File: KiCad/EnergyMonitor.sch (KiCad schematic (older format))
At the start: 70 parts, among them J1 Conn_01x04, J10 AudioJack3_Ground_Switch_5_pin, J11 Conn_01x02, J13 Barrel_Jack_Switch, J14 Conn_01x04, J15 Conn_01x04, J16 4P4C, J2 Conn_01x04, J3 Conn_01x04, J4 Conn_01x04, J5 Conn_01x04, J6 Conn_01x04, J7 Conn_01x02, J8 AudioJack3_Ground_Switch_5_pin, J9 AudioJack3_Ground_Switch_5_pin, U1 ESP32_D1_MINI, U2 HT7333

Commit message: circuit design & pcb layout
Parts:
- R14: footprint LED_SMD:LED_0805_2012Metric -> Resistor_SMD:R_0805_2012Metric
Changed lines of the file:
@@
 F 0 "R14" H 5595 6896 50  0000 L CNN
 F 1 "4K7" H 5595 6805 50  0000 L CNN
-F 2 "LED_SMD:LED_0805_2012Metric" V 5455 6850 50  0001 C CNN
+F 2 "Resistor_SMD:R_0805_2012Metric" V 5455 6850 50  0001 C CNN
 F 3 "~" H 5525 6850 50  0001 C CNN
 	1    5525 6850

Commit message: circuit design & pcb layout
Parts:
- added R15, R30, R31, R32, R33: 0R, Resistor_SMD:R_0805_2012Metric, symbol Device:R
- J14: footprint Connector_JST:JST_SH_SM04B-SRSS-TB_1x04-1MP_P1.00mm_Horizontal -> Connector_JST:JST_SH_BM04B-SRSS-TB_1x04-1MP_P1.00mm_Vertical
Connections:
- net ADC1_CH4: now also U1.7 (IO35); no longer U1.33 (IO32)
- net ADC1_CH5: now also U1.33 (IO32); no longer U1.9 (IO33)
- net ADC1_CH7: now also U1.9 (IO33); no longer U1.7 (IO35)
- net GND: now also J13.2, J13.3, R15.1, R30.1, R31.1, R32.1, R33.1
- net GNDA: now also R15.2, R30.2, R31.2, R32.2, R33.2; no longer J13.2, J13.3
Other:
- note added: "Connector_JST:JST_SH_BM04B-SRSS-TB_1x04-1MP_P1.00mm_Vertical"
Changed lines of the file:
@@
 Sheet 1 1
 Title "ESP32 Energy Monitor"
-Date "2021-09-22"
+Date "2021-09-24"
 Rev "v1.0"
 Comp ""
@@
 Text GLabel 1650 2725 0    50   Input ~ 0
 ADC1_CH6
-Text GLabel 1650 2325 0    50   Input ~ 0
+Text GLabel 1650 2525 0    50   Input ~ 0
 ADC1_CH7
 Text Notes 9850 5200 0    50   ~ 0
@@
 	1    0    0    -1
 $EndComp
-$Comp
-L power:GNDA #PWR024
-U 1 1 613562F0
-P 8325 2400
-F 0 "#PWR024" H 8325 2150 50  0001 C CNN
-F 1 "GNDA" H 8330 2227 50  0000 C CNN
-F 2 "" H 8325 2400 50  0001 C CNN
-F 3 "" H 8325 2400 50  0001 C CNN
-	1    8325 2400
-	1    0    0    -1
-$EndComp
 Wire Wire Line
 	8175 2300 8325 2300
@@
 Text Notes 4000 7550 0    50   ~ 0
 Remove Jumper\nif ESP32 powered\nby USB.
-Text GLabel 1650 2525 0    50   Input ~ 0
-ADC1_CH5
 Text GLabel 2450 2425 2    50   Input ~ 0
+ADC1_CH5
+Text GLabel 1650 2325 0    50   Input ~ 0
 ADC1_CH4
 Text GLabel 2450 2125 2    50   Input ~ 0
@@
 F 0 "J14" H 8580 4842 50  0000 L CNN
 F 1 "Conn_01x04" H 8580 4751 50  0000 L CNN
-F 2 "Connector_JST:JST_SH_SM04B-SRSS-TB_1x04-1MP_P1.00mm_Horizontal" H 8500 4850 50  0001 C CNN
+F 2 "Connector_JST:JST_SH_BM04B-SRSS-TB_1x04-1MP_P1.00mm_Vertical" H 8500 4850 50  0001 C CNN
 F 3 "~" H 8500 4850 50  0001 C CNN
 	1    8500 4850
@@
 Text Notes 5875 7425 0    50   ~ 0
 red superbright LED\n0805 SMD\ngreen band -ve\n1k R => 1.4mA\n4K7 => 0.3mA\n@3.3v
+$Comp
+L power:GND #PWR0106
+U 1 1 6153C70C
+P 8325 2400
+F 0 "#PWR0106" H 8325 2150 50  0001 C CNN
+F 1 "GND" H 8330 2227 50  0000 C CNN
+F 2 "" H 8325 2400 50  0001 C CNN
+F 3 "" H 8325 2400 50  0001 C CNN
+	1    8325 2400
+	1    0    0    -1
+$EndComp
+$Comp
+L power:GND #PWR0107
+U 1 1 61546152
+P 8725 5850
+F 0 "#PWR0107" H 8725 5600 50  0001 C CNN
+F 1 "GND" H 8730 5677 50  0000 C CNN
+F 2 "" H 8725 5850 50  0001 C CNN
+F 3 "" H 8725 5850 50  0001 C CNN
+	1    8725 5850
+	1    0    0    -1
+$EndComp
+$Comp
+L power:GNDA #PWR0108
+U 1 1 61546DE3
+P 8425 5850
+F 0 "#PWR0108" H 8425 5600 50  0001 C CNN
+F 1 "GNDA" H 8430 5677 50  0000 C CNN
+F 2 "" H 8425 5850 50  0001 C CNN
+F 3 "" H 8425 5850 50  0001 C CNN
+	1    8425 5850
+	1    0    0    -1
+$EndComp
+Text Notes 12275 4825 0    50   ~ 0
+Connector_JST:JST_SH_BM04B-SRSS-TB_1x04-1MP_P1.00mm_Vertical
+$Comp
+L Device:R R32
+U 1 1 6154DEF5
+P 8575 5700
+F 0 "R32" V 8575 5375 50  0000 L CNN
+F 1 "0R" V 8575 5650 50  0000 L CNN
+F 2 "Resistor_SMD:R_0805_2012Metric" V 8505 5700 50  0001 C CNN
+F 3 "~" H 8575 5700 50  0001 C CNN
+	1    8575 5700
+	0    1    1    0
+$EndComp
+$Comp
+L Device:R R31
+U 1 1 6154EEF3
+P 8575 5575
+F 0 "R31" V 8575 5250 50  0000 L CNN
+F 1 "0R" V 8575 5525 50  0000 L CNN
+F 2 "Resistor_SMD:R_0805_2012Metric" V 8505 5575 50  0001 C CNN
+F 3 "~" H 8575 5575 50  0001 C CNN
+	1    8575 5575
+	0    1    1    0
+$EndComp
+$Comp
+L Device:R R30
+U 1 1 615542A9
+P 8575 5450
+F 0 "R30" V 8575 5125 50  0000 L CNN
+F 1 "0R" V 8575 5400 50  0000 L CNN
+F 2 "Resistor_SMD:R_0805_2012Metric" V 8505 5450 50  0001 C CNN
+F 3 "~" H 8575 5450 50  0001 C CNN
+	1    8575 5450
+	0    1    1    0
+$EndComp
+$Comp
+L Device:R R15
+U 1 1 61554A8F
+P 8575 5325
+F 0 "R15" V 8575 5000 50  0000 L CNN
+F 1 "0R" V 8575 5275 50  0000 L CNN
+F 2 "Resistor_SMD:R_0805_2012Metric" V 8505 5325 50  0001 C CNN
+F 3 "~" H 8575 5325 50  0001 C CNN
+	1    8575 5325
+	0    1    1    0
+$EndComp
+Wire Wire Line
+	8725 5325 8725 5450
+Wire Wire Line
+	8725 5450 8725 5575
+Connection ~ 8725 5450
+Wire Wire Line
+	8725 5575 8725 5700
+Connection ~ 8725 5575
+Wire Wire Line
+	8725 5700 8725 5850
+Connection ~ 8725 5700
+Wire Wire Line
+	8425 5850 8425 5700
+Wire Wire Line
+	8425 5700 8425 5575
+Connection ~ 8425 5700
+Wire Wire Line
+	8425 5575 8425 5450
+Connection ~ 8425 5575
+Wire Wire Line
+	8425 5450 8425 5325
+Connection ~ 8425 5450
+$Comp
+L Device:R R33
+U 1 1 615B1549
+P 8575 5200
+F 0 "R33" V 8575 4875 50  0000 L CNN
+F 1 "0R" V 8575 5150 50  0000 L CNN
+F 2 "Resistor_SMD:R_0805_2012Metric" V 8505 5200 50  0001 C CNN
+F 3 "~" H 8575 5200 50  0001 C CNN
+	1    8575 5200
+	0    1    1    0
+$EndComp
+Wire Wire Line
+	8725 5200 8725 5325
+Connection ~ 8725 5325
+Wire Wire Line
+	8425 5200 8425 5325
+Connection ~ 8425 5325
 $EndSCHEMATC

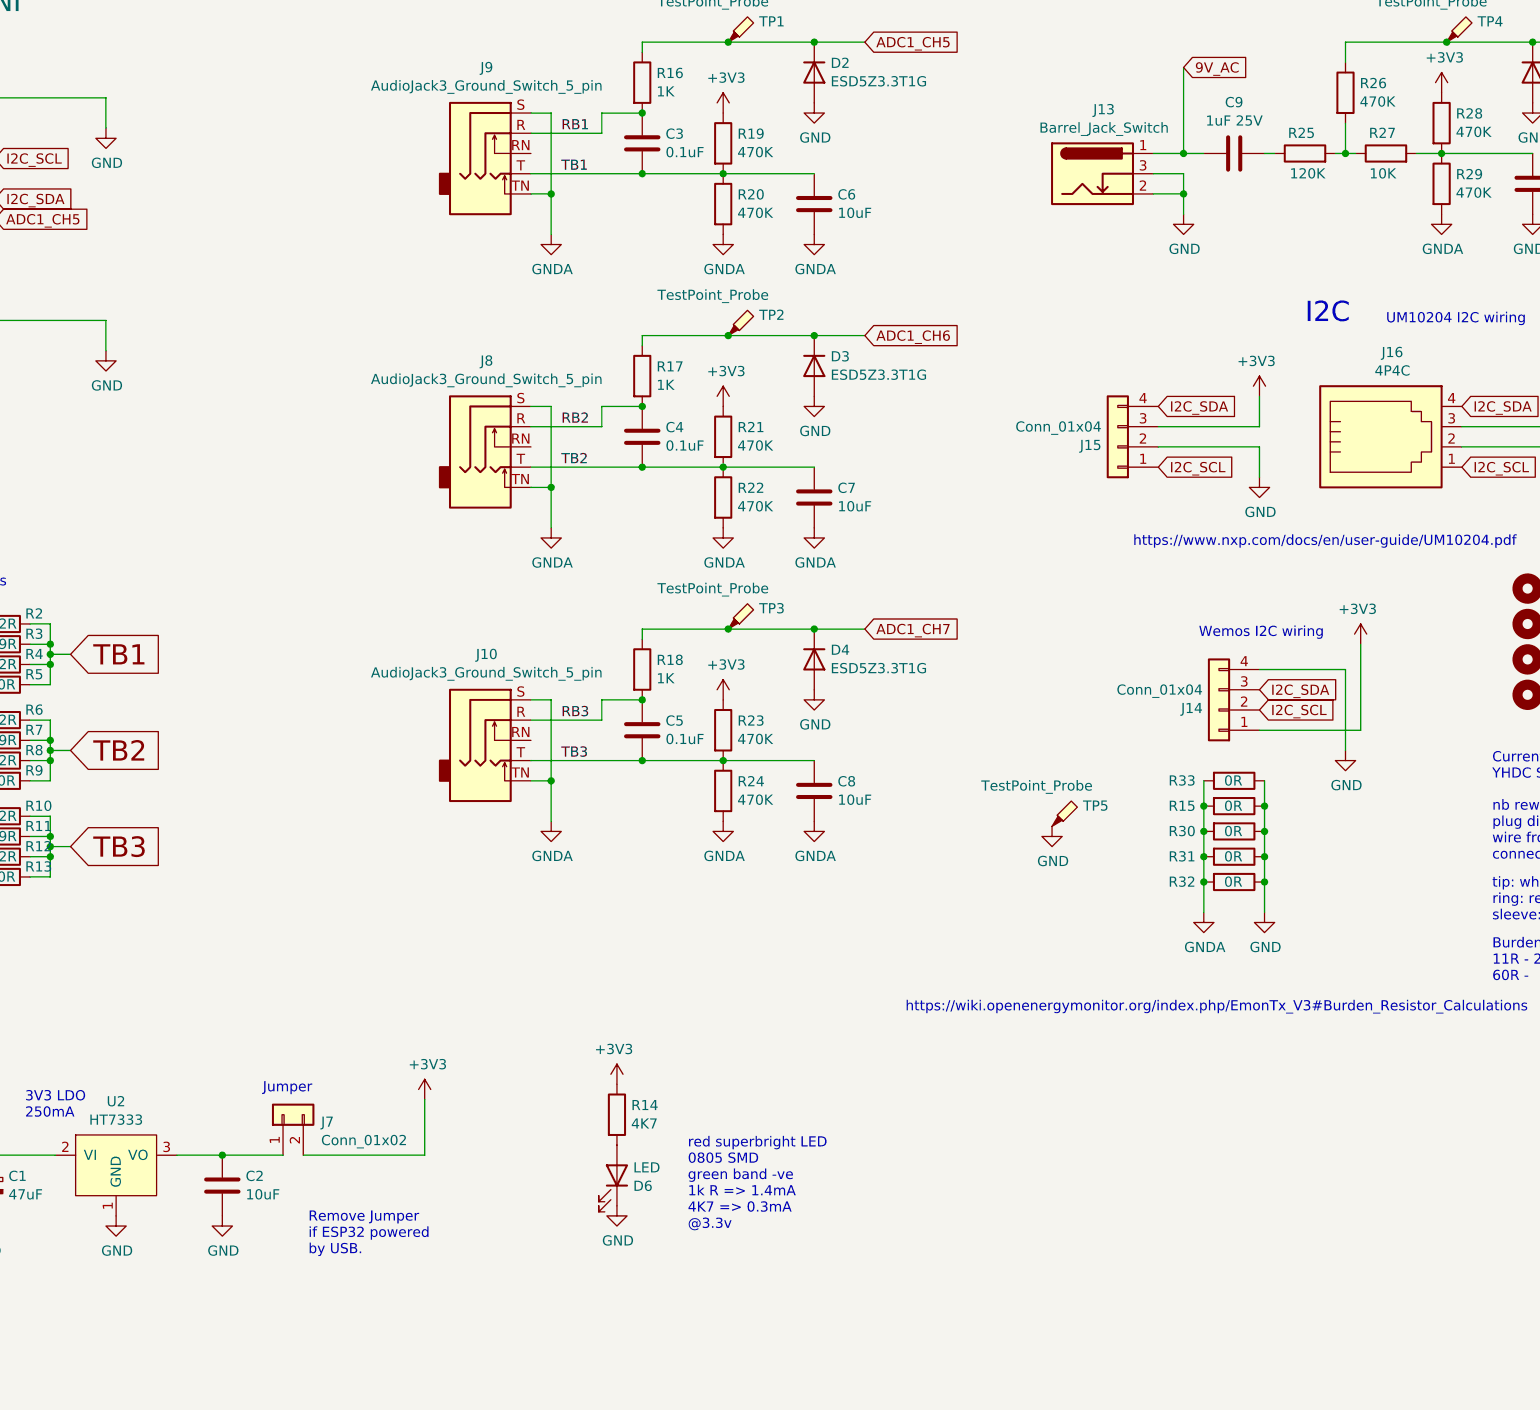
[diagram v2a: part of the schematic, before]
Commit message: added 2nd I2C port
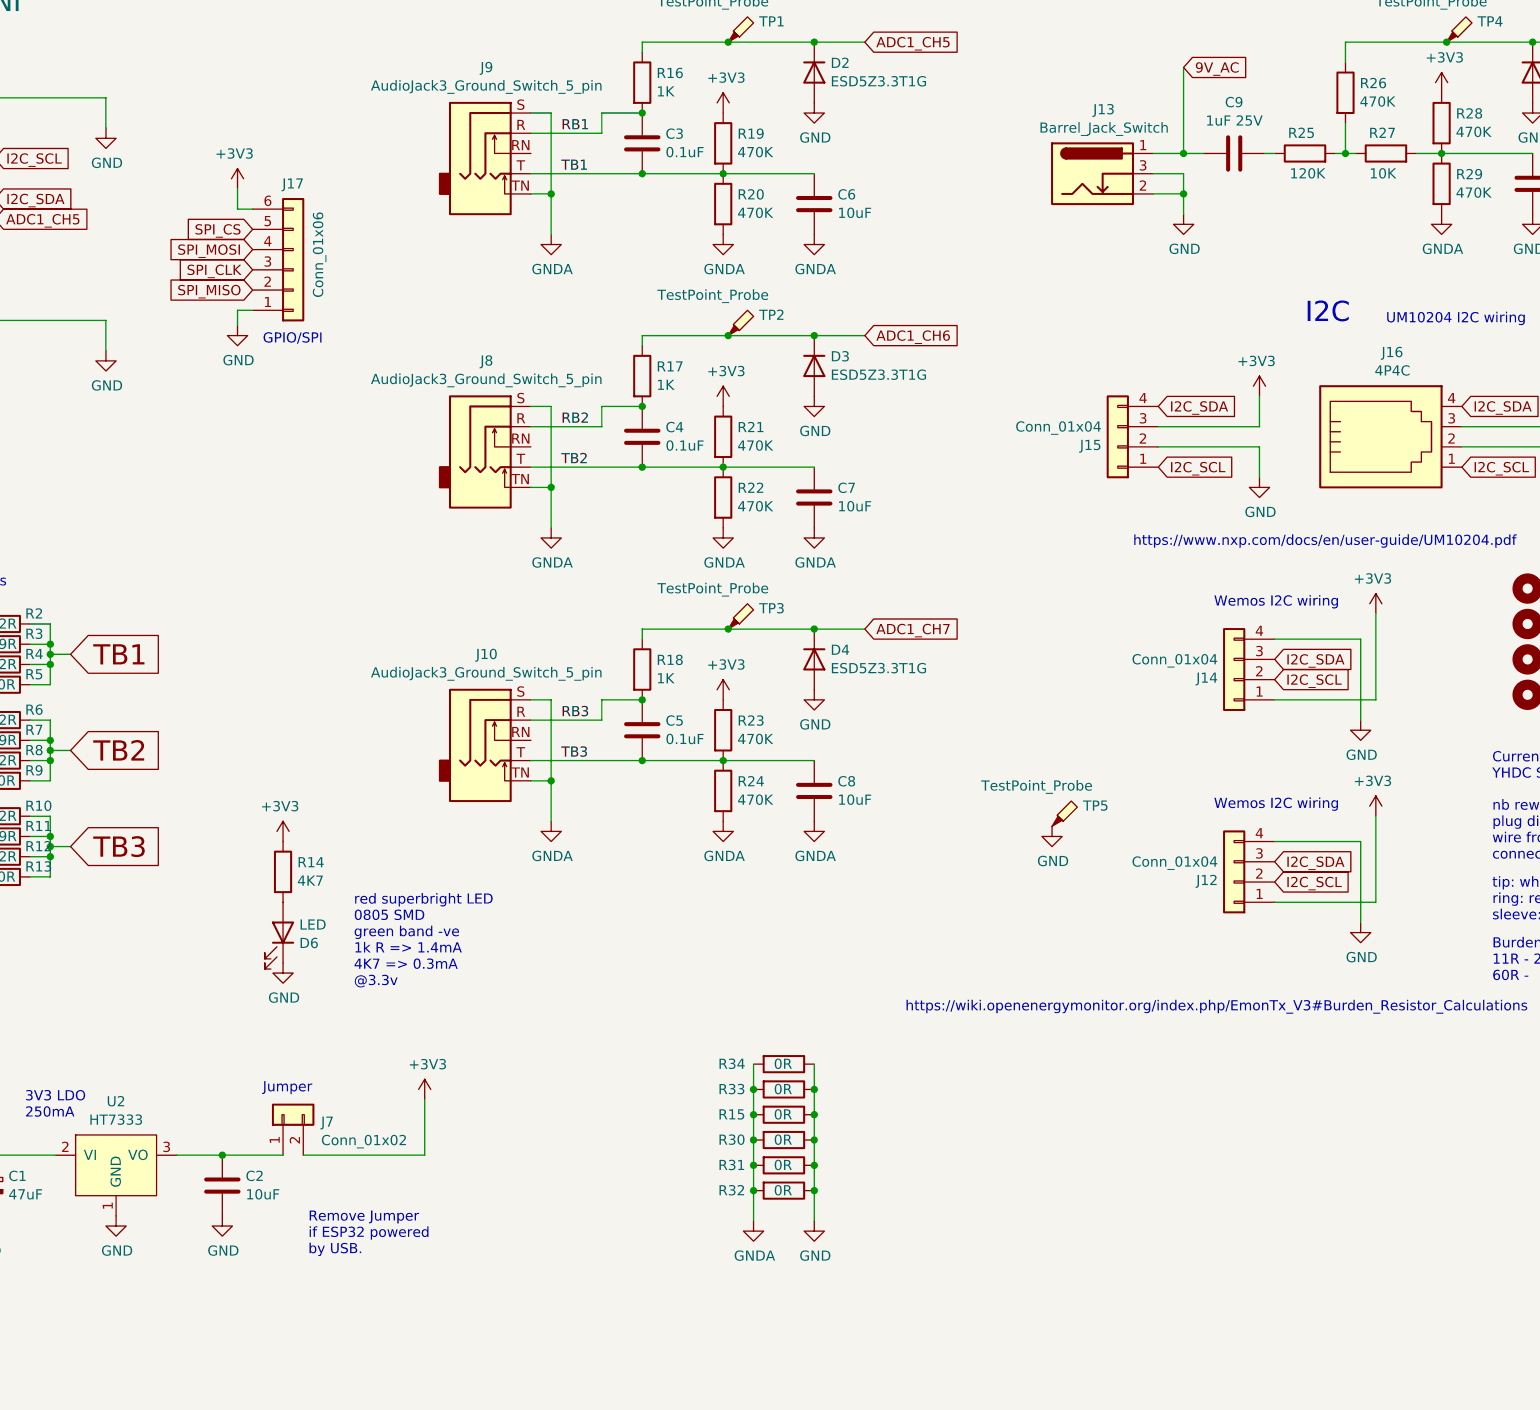
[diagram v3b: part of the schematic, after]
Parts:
- added J12: Conn_01x04, Connector_JST:JST_SH_SM04B-SRSS-TB_1x04-1MP_P1.00mm_Horizontal, symbol Connector_Generic:Conn_01x04
- added J17: Conn_01x06, symbol Connector_Generic:Conn_01x06
- added R34: 0R, Resistor_SMD:R_0805_2012Metric, symbol Device:R
- C1: footprint Capacitor_SMD:CP_Elec_5x4.4 -> Capacitor_SMD:CP_Elec_6.3x5.9
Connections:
- net +3V3: now also J12.1 (Pin_1), J17.6 (Pin_6)
- net GND: now also J12.4 (Pin_4), J17.1 (Pin_1), R34.1
- net GNDA: now also R34.2
- net I2C_SCL: now also J12.2 (Pin_2)
- net I2C_SDA: now also J12.3 (Pin_3)
- net SPI_CLK: now also J17.3 (Pin_3)
- net SPI_CS: now also J17.5 (Pin_5)
- net SPI_MISO: now also J17.2 (Pin_2)
- net SPI_MOSI: now also J17.4 (Pin_4)
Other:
- note added: "GPIO/SPI"
- moved on the sheet: D6, J14, R14, R15, R30, R31, R32, R33

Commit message: added GPIO/SPI port
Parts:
- J17: footprint (none) -> Connector_PinHeader_2.54mm:PinHeader_1x06_P2.54mm_Vertical
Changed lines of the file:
@@
 Sheet 1 1
 Title "ESP32 Energy Monitor"
-Date "2021-09-24"
+Date "2021-09-25"
 Rev "v1.0"
 Comp ""
@@
 F 0 "J17" H 3925 2250 50  0000 C CNN
 F 1 "Conn_01x06" V 4050 2600 50  0000 C CNN
-F 2 "" H 3925 2675 50  0001 C CNN
+F 2 "Connector_PinHeader_2.54mm:PinHeader_1x06_P2.54mm_Vertical" H 3925 2675 50  0001 C CNN
 F 3 "~" H 3925 2675 50  0001 C CNN
 	1    3925 2675

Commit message: fabrication gerbers v1.0
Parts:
- added C11: 10uF, Capacitor_SMD:CP_Elec_6.3x5.9, symbol Device:CP
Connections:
- net GND: now also C11.2
- net at C2.1, J7.1 (Pin_1), U2.3 (VO): now also C11.1
- no-connect marks 0 -> 28
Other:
- note added: "H7333 Input voltage 12V\nabsolute maximum 14V"
- note added: "Test this !!!"
- note added: "provision for electrolytic\noutput capacitor?"
- moved on the sheet: J7
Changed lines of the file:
@@
 L Connector_Generic:Conn_01x02 J7
 U 1 1 613318AE
-P 3875 6850
-F 0 "J7" V 3839 6662 50  0000 R CNN
-F 1 "Conn_01x02" V 3748 6662 50  0000 R CNN
-F 2 "Connector_PinHeader_2.54mm:PinHeader_1x02_P2.54mm_Vertical" H 3875 6850 50  0001 C CNN
-F 3 "~" H 3875 6850 50  0001 C CNN
-	1    3875 6850
+P 4350 6850
+F 0 "J7" V 4314 6662 50  0000 R CNN
+F 1 "Conn_01x02" V 4223 6662 50  0000 R CNN
+F 2 "Connector_PinHeader_2.54mm:PinHeader_1x02_P2.54mm_Vertical" H 4350 6850 50  0001 C CNN
+F 3 "~" H 4350 6850 50  0001 C CNN
+	1    4350 6850
 	0    -1   -1   0
 $EndComp
@@
 	3350 7050 3575 7050
 Wire Wire Line
-	3575 7050 3875 7050
+	3575 7050 4100 7050
 Connection ~ 3575 7050
 $Comp
@@
 L power:+3V3 #PWR08
 U 1 1 61337478
-P 4575 6775
-F 0 "#PWR08" H 4575 6625 50  0001 C CNN
-F 1 "+3V3" H 4590 6948 50  0000 C CNN
-F 2 "" H 4575 6775 50  0001 C CNN
-F 3 "" H 4575 6775 50  0001 C CNN
-	1    4575 6775
+P 5050 6775
+F 0 "#PWR08" H 5050 6625 50  0001 C CNN
+F 1 "+3V3" H 5065 6948 50  0000 C CNN
+F 2 "" H 5050 6775 50  0001 C CNN
+F 3 "" H 5050 6775 50  0001 C CNN
+	1    5050 6775
 	1    0    0    -1
 $EndComp
 Wire Wire Line
-	3975 7050 4575 7050
+	4450 7050 5050 7050
 Wire Wire Line
-	4575 7050 4575 6775
-Text Notes 3775 6750 0    50   ~ 0
+	5050 7050 5050 6775
+Text Notes 4250 6750 0    50   ~ 0
 Jumper
 Text Notes 1250 6600 0    100  ~ 0
@@
 Text Notes 1250 7500 0    50   ~ 0
 check these values !!
-Text Notes 4000 7550 0    50   ~ 0
+Text Notes 4275 6625 0    50   ~ 0
 Remove Jumper\nif ESP32 powered\nby USB.
 Text GLabel 2450 2425 2    50   Input ~ 0
@@
 Wire Wire Line
 	10200 3450 10200 3300
-Text GLabel 10350 3550 2    50   Input ~ 0
-GND
-Text GLabel 10350 3450 2    50   Input ~ 0
-+3V3
 $Comp
 L power:GND #PWR018
@@
 Text Notes 3775 3050 0    50   ~ 0
 GPIO/SPI
+Text Notes 2525 6400 0    50   ~ 0
+H7333  Input voltage 12V\nabsolute maximum 14V
+Text Notes 2525 6525 0    50   ~ 0
+Test this !!!
+$Comp
+L Device:CP C11
+U 1 1 615002E0
+P 4100 7200
+F 0 "C11" H 4218 7246 50  0000 L CNN
+F 1 "10uF" H 4218 7155 50  0000 L CNN
+F 2 "Capacitor_SMD:CP_Elec_6.3x5.9" H 4138 7050 50  0001 C CNN
+F 3 "~" H 4100 7200 50  0001 C CNN
+	1    4100 7200
+	1    0    0    -1
+$EndComp
+Connection ~ 4100 7050
+Wire Wire Line
+	4100 7050 4350 7050
+$Comp
+L power:GND #PWR0113
+U 1 1 6150D208
+P 4100 7350
+F 0 "#PWR0113" H 4100 7100 50  0001 C CNN
+F 1 "GND" H 4105 7177 50  0000 C CNN
+F 2 "" H 4100 7350 50  0001 C CNN
+F 3 "" H 4100 7350 50  0001 C CNN
+	1    4100 7350
+	1    0    0    -1
+$EndComp
+Text Notes 4225 7475 0    50   ~ 0
+provision for electrolytic\noutput capacitor?
+Wire Notes Line
+	3950 7000 4225 7000
+Wire Notes Line
+	4225 7000 4225 7100
+Wire Notes Line
+	4225 7100 4450 7100
+Wire Notes Line
+	4450 7100 4450 7250
+Wire Notes Line
+	4450 7250 5200 7250
+Wire Notes Line
+	5200 7250 5200 7600
+Wire Notes Line
+	5200 7600 3950 7600
+Wire Notes Line
+	3950 7600 3950 7000
+NoConn ~ 2450 1725
+NoConn ~ 2450 1925
+NoConn ~ 2450 2025
+NoConn ~ 1650 1825
+NoConn ~ 1650 2025
+NoConn ~ 1650 2125
+NoConn ~ 1650 2225
+NoConn ~ 2450 2225
+NoConn ~ 2450 2625
+NoConn ~ 2450 2725
+NoConn ~ 2450 2825
+NoConn ~ 1650 2925
+NoConn ~ 1650 3100
+NoConn ~ 1650 3325
+NoConn ~ 1650 3425
+NoConn ~ 1650 3525
+NoConn ~ 1650 3625
+NoConn ~ 2450 3625
+NoConn ~ 2450 3525
+NoConn ~ 2450 3425
+NoConn ~ 2450 3325
+NoConn ~ 2450 3225
+NoConn ~ 2450 3125
+NoConn ~ 2450 3025
+NoConn ~ 5100 3550
+NoConn ~ 5100 2100
+NoConn ~ 5100 5000
+NoConn ~ 2450 2525
 $EndSCHEMATC
